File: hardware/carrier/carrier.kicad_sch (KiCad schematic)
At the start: 153 parts, among them J1 Harness_4Runner, J2 Pi 4 GPIO, J3 UART, M1 FAN1, M2 FAN2, Q1 BUK7Y4R8-60E, Q2 BUK7Y4R8-60E, Q3 MMBT3904, Q4 MMBT3904, Q5 MMBT3904, Q6 2N7002, Q7 2N7002, U1 LM74800-Q1, U2 ADS1115IDGS, U3 DS3231SN, U4 CAT24C32, U5 LM61460-Q1, U6 TLV75533PDBV, U7 TAS6424E-Q1, U8 CS2100-CP, Y1 12MHz

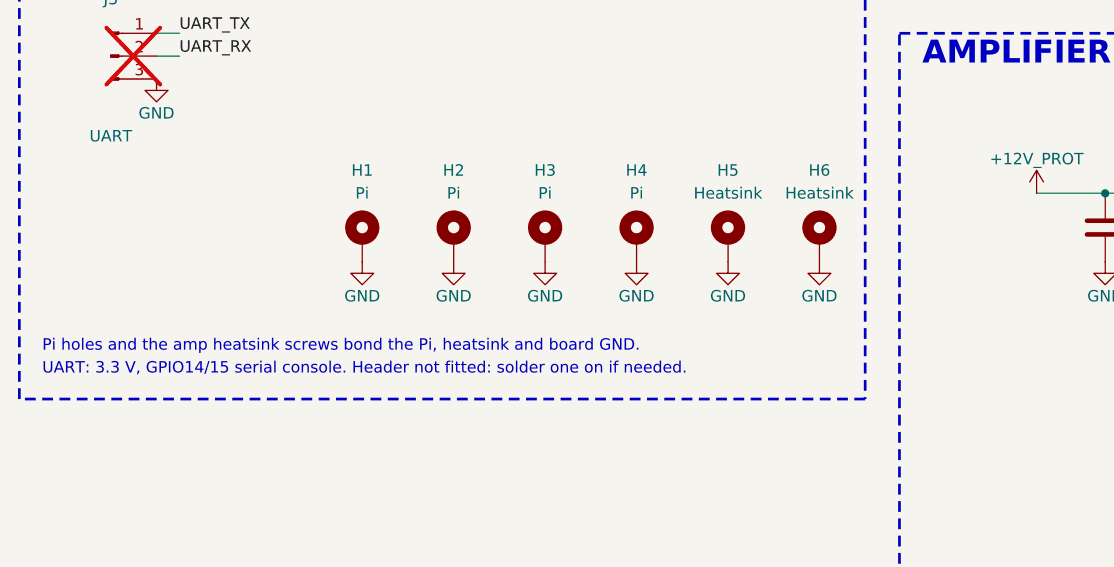
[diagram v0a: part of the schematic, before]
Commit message: Carrier PCB: Pi geometry from the HAT spec, amplifier block placement
J2 sits on the bottom with pin 1 over the Pi's pin 1 (checked by pad
position), H1-H4 on the Pi hole pattern and isolated per the HAT spec,
USB/Ethernet notch and display-flex cutout follow the Pi's position
(provisional until measured). The TAS6424 block follows TI's EVM layout.
Parts carry a Section field so placement finds them by block and net.
Boot caps move to 0603 to fit the 0.635 mm pitch.

Co-Authored-By: Claude Opus 5.5 <noreply@anthropic.com>
Claude-Session: https://claude.ai/code/session_01EoLoLi7g91W5u4w3UzwQgu
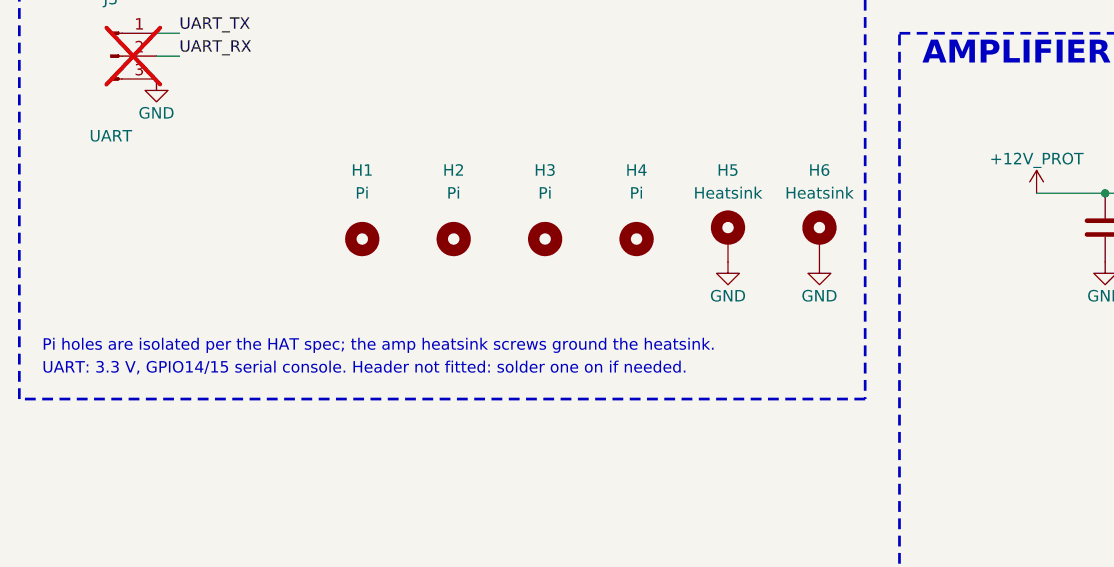
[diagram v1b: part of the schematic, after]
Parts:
- BT1, C10, C11, JP1, R11, R12, R13, R14, TP1, U3, U4: Section (none) -> rtc
- C1, C2, C3, C4, C5, D1, Q1, Q2, R1, R2, R3, R4, U1: Section (none) -> protection
- C12, C13, C14, C15, D4, D5, D6, Q3, Q4, Q5, R15, R16, R17, R18, R19, R20, R21, R22, R23, R24, R25, R26: Section (none) -> hold
- C16, C17, C18, C19, C20, C21, C22, C23, C24, C25, C26, C27, C28, L1, R27, R28, R29, R30, R31, R32, R33, U5, U6: Section (none) -> buck
- C29, C30, C31, C32, C33, C34, C35, C36, C37, C38, C39, C40, C41, C42, U7: Section (none) -> amp
- C43, C44, C45, C46, C47, C48, C49, C50: footprint Capacitor_SMD:C_0805_2012Metric -> Capacitor_SMD:C_0603_1608Metric; LCSC C28323 -> C5199872; MPN CL21B105KBFNNNE -> CL10B105KB8NQNC; Section (none) -> amp
- C51, C52, C53, C54, C55, C56, C57, C58, C59, C60, C61, C62, C63, C64, C65, C66, L2, L3, L4, L5, L6, L7, L8, L9: Section (none) -> filter
- C6, C7, C8, C9, D2, D3, R10, R5, R6, R7, R8, R9, U2: Section (none) -> swc
- C67, C68, C69, R38, R39, U8, Y1: Section (none) -> clock
- H1, H2, H3, H4: footprint MountingHole:MountingHole_2.7mm_M2.5_Pad_Via -> MountingHole:MountingHole_2.7mm_M2.5; symbol Mechanical:MountingHole_Pad -> Mechanical:MountingHole; Section (none) -> misc
- H5, H6, J3: Section (none) -> misc
- J1: Section (none) -> harness
- J2: Section (none) -> pi
- M1, M2, Q6, Q7, R34, R35, R36, R37: Section (none) -> fans
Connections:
- net GND: no longer H1.1, H2.1, H3.1, H4.1
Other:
- note added: "Pi holes are isolated per the HAT spec; the amp heatsink screws ground the heatsink."
- note removed: "Pi holes and the amp heatsink screws bond the Pi, heatsink and board GND."

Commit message: Carrier PCB: place the remaining circuits; every part on the board
RTC, coin cell and ID EEPROM over the Pi, key/lights/reverse sensing and
the wheel ADC beside J1's control pins, fan headers on the bottom edge.
U8 uses the 3x3 TSSOP-10 land pattern (same MO-187 package, wider gaps).
DRC: no overlaps or clearance errors; routing still to do.

Co-Authored-By: Claude Opus 5.5 <noreply@anthropic.com>
Claude-Session: https://claude.ai/code/session_01EoLoLi7g91W5u4w3UzwQgu
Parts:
- U8: footprint Package_SO:MSOP-10_3x3mm_P0.5mm -> Package_SO:TSSOP-10_3x3mm_P0.5mm

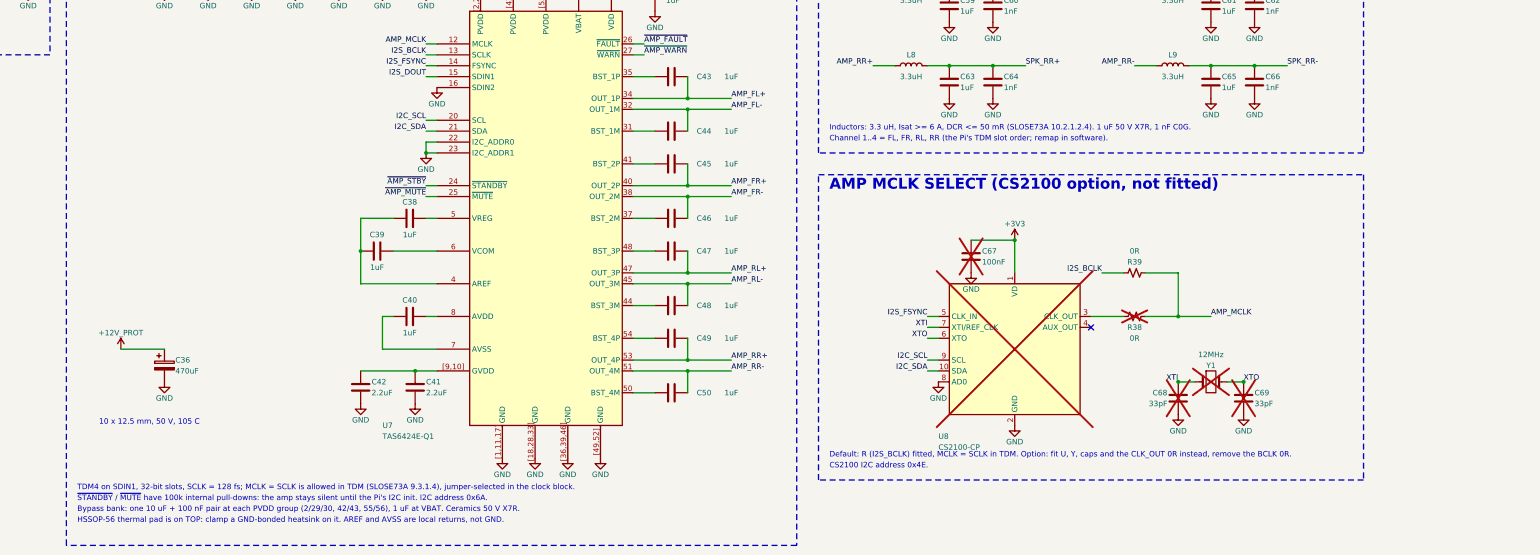
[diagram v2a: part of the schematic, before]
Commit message: Carrier: board becomes the I2S clock master; amp heatsink design
The Pi's PCM block carries only two channels, so TDM4 cannot feed four
amp channels, and the TAS6424 needs a real MCLK (128-512 fs) outside
TDM. A 12.288 MHz oscillator now drives the amp's MCLK and a PCM1808-Q1
in master mode (MD1 = MD0 = 1) divides it to BCK = 64 fs and LRCK =
48 kHz; the Pi runs its I2S port as a clock consumer. SDIN2 takes the
same data as SDIN1, so the rear speakers play the front stereo pair and
the amp's per-channel volume does the fader. The commercial-grade
CS2100 option is gone.

tools/heatsink.py models a CNC aluminium heatsink after TI's EVM part
(20 x 41.4 mm, four 25 mm fins, feet on the grounded screw pads, M3
tapped from below); its outline is drawn on the board so nothing taller
than 2.2 mm sits under it.

Co-Authored-By: Claude Opus 5.5 <noreply@anthropic.com>
Claude-Session: https://claude.ai/code/session_01EoLoLi7g91W5u4w3UzwQgu
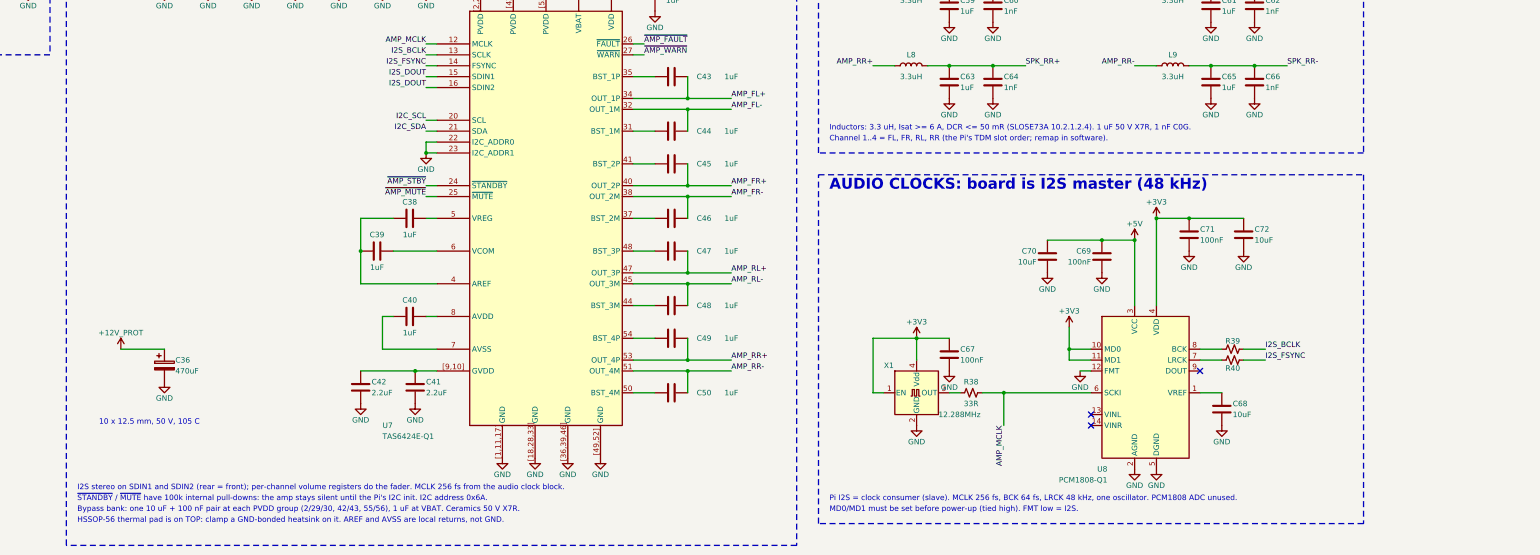
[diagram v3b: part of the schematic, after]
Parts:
- removed Y1: 12MHz, Crystal:Crystal_SMD_3225-4Pin_3.2x2.5mm, symbol Device:Crystal
- added C70, C72: 10uF, Capacitor_SMD:C_0805_2012Metric, symbol Device:C
- added C71: 100nF, Capacitor_SMD:C_0603_1608Metric, symbol Device:C
- added R40: 33R, Resistor_SMD:R_0603_1608Metric, symbol Device:R_Small_US
- added X1: 12.288MHz, Oscillator:Oscillator_SMD_Abracon_ASE-4Pin_3.2x2.5mm, symbol Oscillator:ASE-xxxMHz
- C67: now fitted
- C68: value 33pF -> 10uF; footprint Capacitor_SMD:C_0603_1608Metric -> Capacitor_SMD:C_0805_2012Metric; LCSC C1663 -> C15850; MPN CL10C330JB8NNNC -> CL21A106KAYNNNE; now fitted
- C69: value 33pF -> 100nF; LCSC C1663 -> C14663; MPN CL10C330JB8NNNC -> CC0603KRX7R9BB104; Manufacturer Samsung Electro-Mechanics -> YAGEO; now fitted
- R38: value 0R -> 33R; LCSC C21189 -> C23140; MPN 0603WAF0000T5E -> 0603WAF330JT5E; now fitted
- R39: value 0R -> 33R; LCSC C21189 -> C23140; MPN 0603WAF0000T5E -> 0603WAF330JT5E
- U8: value CS2100-CP -> PCM1808-Q1; footprint Package_SO:TSSOP-10_3x3mm_P0.5mm -> Package_SO:TSSOP-14_4.4x5mm_P0.65mm; symbol carrier:CS2100-CP -> carrier:PCM1808-Q1; LCSC C2663267 -> C2864157; MPN CS2100CP-CZZR -> PCM1808QPWRQ1; Manufacturer Cirrus Logic -> Texas Instruments; now fitted
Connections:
- net +3V3: now also U8.10 (MD0), U8.11 (MD1), U8.4 (VDD), C71.1, C72.1, X1.1 (EN), X1.4 (Vdd); no longer U8.1 (VD)
- net +5V: now also C69.1, U8.3 (VCC), C70.1
- net AMP_MCLK: now also U8.6 (SCKI); no longer R39.2
- net GND: now also U8.12 (FMT), U8.5 (DGND), C70.2, C71.2, C72.2, X1.2 (GND); no longer U7.16 (SDIN2), U8.8 (AD0)
- net I2C_SCL: no longer U8.9 (SCL)
- net I2C_SDA: no longer U8.10 (SDA)
- net I2S_BCLK: now also R39.2; no longer R39.1
- net I2S_DOUT: now also U7.16 (SDIN2)
- net I2S_FSYNC: now also R40.2; no longer U8.5 (CLK_IN)
- net at R38.1: now also X1.3 (OUT); no longer U8.3 (CLK_OUT)
- net XTI: no longer names the net of C68.1
- net XTI: now also U8.1 (VREF); no longer U8.7 (XTI/REF_CLK)
- removed net XTO: C69.1, U8.6 (XTO)
- new net: R39.1, U8.8 (BCK)
- new net: R40.1, U8.7 (LRCK)
- no-connect marks 13 -> 15
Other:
- note added: "AUDIO CLOCKS: board is I2S master (48 kHz)"
- note added: "I2S stereo on SDIN1 and SDIN2 (rear = front); per-channel volume registers do the fader. MCLK 256 fs from the audio clock block."
- note added: "MD0/MD1 must be set before power-up (tied high). FMT low = I2S."
- note added: "Pi I2S = clock consumer (slave). MCLK 256 fs, BCK 64 fs, LRCK 48 kHz, one oscillator. PCM1808 ADC unused."
- note removed: "AMP MCLK SELECT (CS2100 option, not fitted)"
- note removed: "CS2100 I2C address 0x4E."
- note removed: "Default: R (I2S_BCLK) fitted, MCLK = SCLK in TDM. Option: fit U, Y, caps and the CLK_OUT 0R instead, remove the BCLK 0R."
- note removed: "TDM4 on SDIN1, 32-bit slots, SCLK = 128 fs; MCLK = SCLK is allowed in TDM (SLOSE73A 9.3.1.4), jumper-selected in the clock block."
- moved on the sheet: R39

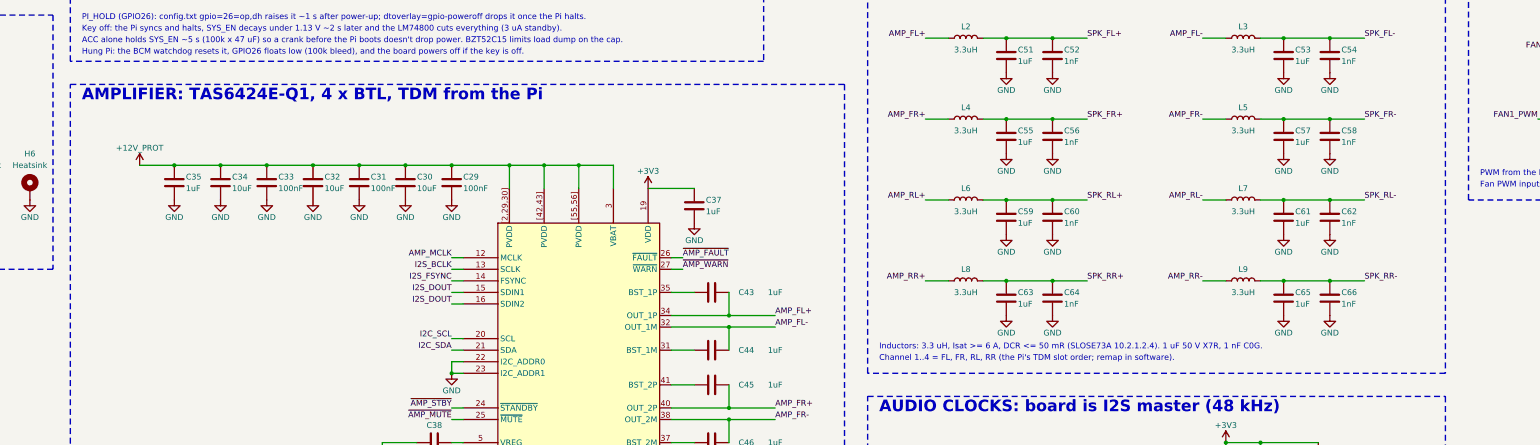
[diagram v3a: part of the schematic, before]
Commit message: Carrier: document the board before routing
hardware/carrier/README.md covers each circuit block and why it was
chosen, the Pi position and where that number came from, the stack-up,
harness wiring, the GPIO map, the shopping list, regeneration commands,
verification status and open items. The root README and INFO.md now
point to it. Two amp schematic notes still described the old TDM plan
and now match the I2S clock-master design. TI's EVM guide is added to
datasheets/.

Co-Authored-By: Claude Opus 5.5 <noreply@anthropic.com>
Claude-Session: https://claude.ai/code/session_01EoLoLi7g91W5u4w3UzwQgu
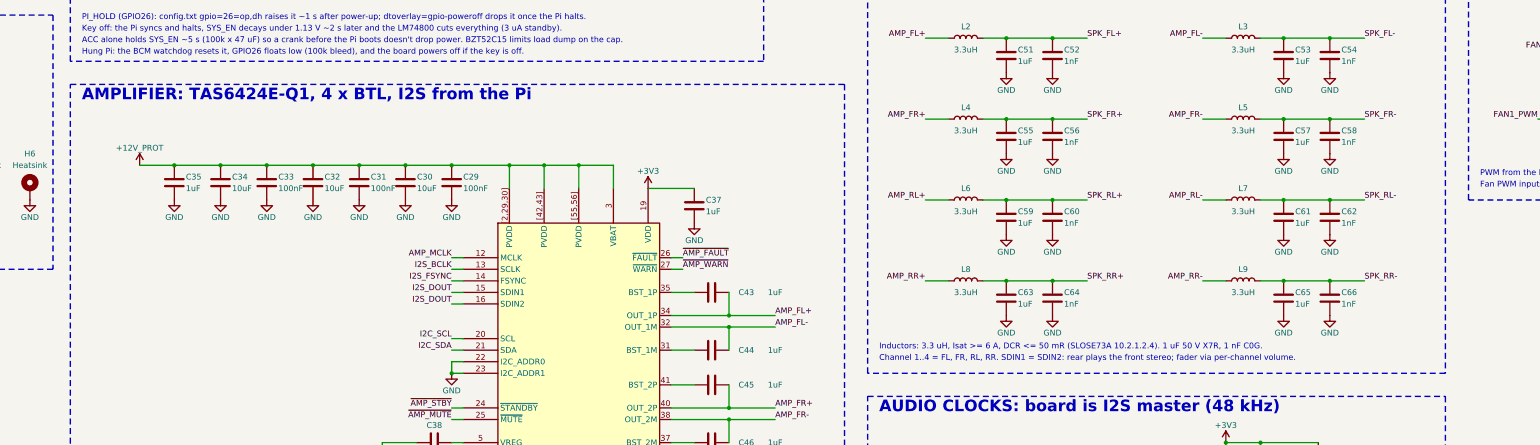
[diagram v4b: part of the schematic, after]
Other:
- note added: "AMPLIFIER: TAS6424E-Q1, 4 x BTL, I2S from the Pi"
- note added: "Channel 1..4 = FL, FR, RL, RR. SDIN1 = SDIN2: rear plays the front stereo; fader via per-channel volume."
- note removed: "AMPLIFIER: TAS6424E-Q1, 4 x BTL, TDM from the Pi"
- note removed: "Channel 1..4 = FL, FR, RL, RR (the Pi's TDM slot order; remap in software)."

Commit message: Carrier: route the board
Four layers: In1 solid GND, In2 split between +12V_PROT and +5V. Power
paths are pours and hand-placed tracks (battery path, buck loop, amp
PVDD, the Pi's 5 V pins); the amp outputs and speaker tracks are routed
by script, P legs on top and M legs under the coils, speaker lanes
nested so none cross. Every GND pad has its own via to the plane. The
rest goes through Freerouting, with a small grid router for the tight
spots. Nothing copper within 3 mm of the outer edge, so a small error in
the Pi position only moves the outline. DRC: 0 errors, 0 unrouted.

Changes made along the way:
- amp channels remapped (ch1..4 = RL, RR, FL, FR) and the harness
  speaker pins reordered (3/13 FR, 4/14 FL, 5/15 RR, 6/16 RL) so the
  speaker tracks run straight; tas6424.py follows
- P-leg boot caps turned and all eight centred on their pin pairs
- coils moved up to open room for the output escapes; centre PVDD caps
  and the 470 uF bulk moved
- LM74800 turned 180 degrees so each pin row faces its parts; C4, C5
  and the OV divider rearranged to match
- fan tach pull-ups moved beside the Pi header
- net classes were being dropped when the board was saved; fixed

tools/build_board.sh rebuilds everything. tools/fit_plate.py makes a
printable plate to check the fit on the screen before ordering.

Co-Authored-By: Claude Opus 5.5 <noreply@anthropic.com>
Claude-Session: https://claude.ai/code/session_01EoLoLi7g91W5u4w3UzwQgu
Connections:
- net AMP_FL+: now also C47.2, L6.1, U7.47 (OUT_3P); no longer C43.2, L2.1, U7.34 (OUT_1P)
- net AMP_FL-: now also C48.2, L7.1, U7.45 (OUT_3M); no longer C44.2, L3.1, U7.32 (OUT_1M)
- net AMP_FR+: now also C49.2, L8.1, U7.53 (OUT_4P); no longer C45.2, L4.1, U7.40 (OUT_2P)
- net AMP_FR-: now also C50.2, L9.1, U7.51 (OUT_4M); no longer C46.2, L5.1, U7.38 (OUT_2M)
- net AMP_RL+: now also C43.2, L2.1, U7.34 (OUT_1P); no longer C47.2, L6.1, U7.47 (OUT_3P)
- net AMP_RL-: now also C44.2, L3.1, U7.32 (OUT_1M); no longer C48.2, L7.1, U7.45 (OUT_3M)
- net AMP_RR+: now also C45.2, L4.1, U7.40 (OUT_2P); no longer C49.2, L8.1, U7.53 (OUT_4P)
- net AMP_RR-: now also C46.2, L5.1, U7.38 (OUT_2M); no longer C50.2, L9.1, U7.51 (OUT_4M)
- net SPK_FL+: now also C59.1, C60.1, J1.4 (SPK_FL+), L6.2; no longer C51.1, C52.1, J1.3 (SPK_FL+), L2.2
- net SPK_FL-: now also C61.1, C62.1, J1.14 (SPK_FL-), L7.2; no longer C53.1, C54.1, J1.13 (SPK_FL-), L3.2
- net SPK_FR+: now also C63.1, C64.1, J1.3 (SPK_FR+), L8.2; no longer C55.1, C56.1, J1.4 (SPK_FR+), L4.2
- net SPK_FR-: now also C65.1, C66.1, J1.13 (SPK_FR-), L9.2; no longer C57.1, C58.1, J1.14 (SPK_FR-), L5.2
- net SPK_RL+: now also C51.1, C52.1, J1.6 (SPK_RL+), L2.2; no longer C59.1, C60.1, J1.5 (SPK_RL+), L6.2
- net SPK_RL-: now also C53.1, C54.1, J1.16 (SPK_RL-), L3.2; no longer C61.1, C62.1, J1.15 (SPK_RL-), L7.2
- net SPK_RR+: now also C55.1, C56.1, J1.5 (SPK_RR+), L4.2; no longer C63.1, C64.1, J1.6 (SPK_RR+), L8.2
- net SPK_RR-: now also C57.1, C58.1, J1.15 (SPK_RR-), L5.2; no longer C65.1, C66.1, J1.16 (SPK_RR-), L9.2
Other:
- note added: "Channel 1..4 = RL, RR, FL, FR (matches J1 order on the board). SDIN1 = SDIN2; fader via per-channel volume."
- note removed: "Channel 1..4 = FL, FR, RL, RR. SDIN1 = SDIN2: rear plays the front stereo; fader via per-channel volume."
